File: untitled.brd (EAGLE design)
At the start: 54 x 54 mm, 22 parts, among them IC1 SN65220DBV, J3 CORTEX_DEBUG_PTH, J6 USB-MICROB, U1 ATSAMD21G-M, U2 MIC5501-3.0YM5-TR

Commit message: added vias below bus connectors
added vias below bus connectors to improve mechanical stability. Added ground symbol on bus connection net.
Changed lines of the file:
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@@
 <wire x1="41.1" y1="10" x2="41.07" y2="9.97" width="0.254" layer="16"/>
+</signal>
+<signal name="N$2">
+<via x="51.45" y="39.2" extent="1-16" drill="0.35"/>
+</signal>
+<signal name="N$3">
+<via x="52.5" y="39.2" extent="1-16" drill="0.35"/>
+</signal>
+<signal name="N$5">
+<via x="51.45" y="44.8" extent="1-16" drill="0.35"/>
+</signal>
+<signal name="N$6">
+<via x="52.5" y="44.8" extent="1-16" drill="0.35"/>
+</signal>
+<signal name="N$7">
+<via x="1.5" y="44.8" extent="1-16" drill="0.35"/>
+</signal>
+<signal name="N$8">
+<via x="2.55" y="44.8" extent="1-16" drill="0.35"/>
+</signal>
+<signal name="N$9">
+<via x="1.5" y="39.2" extent="1-16" drill="0.35"/>
+</signal>
+<signal name="N$11">
+<via x="2.55" y="39.2" extent="1-16" drill="0.35"/>
 </signal>
 </signals>

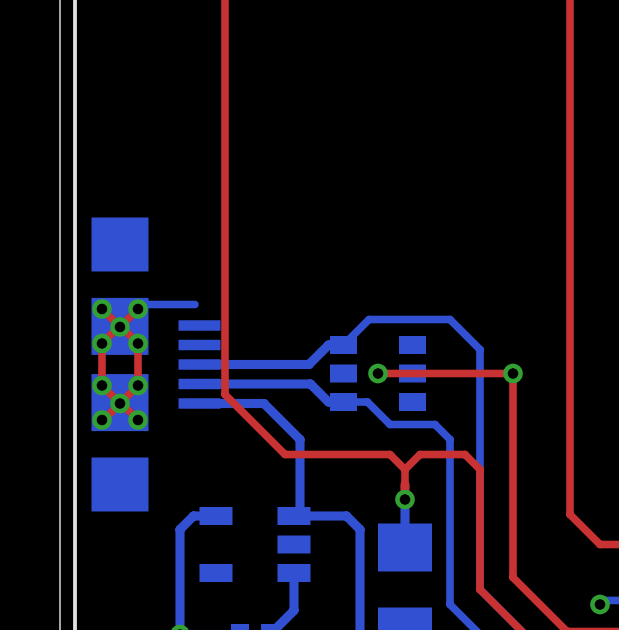
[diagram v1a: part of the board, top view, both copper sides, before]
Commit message: fixed wire stub drc error
removed wire stub on the USB connection vias.
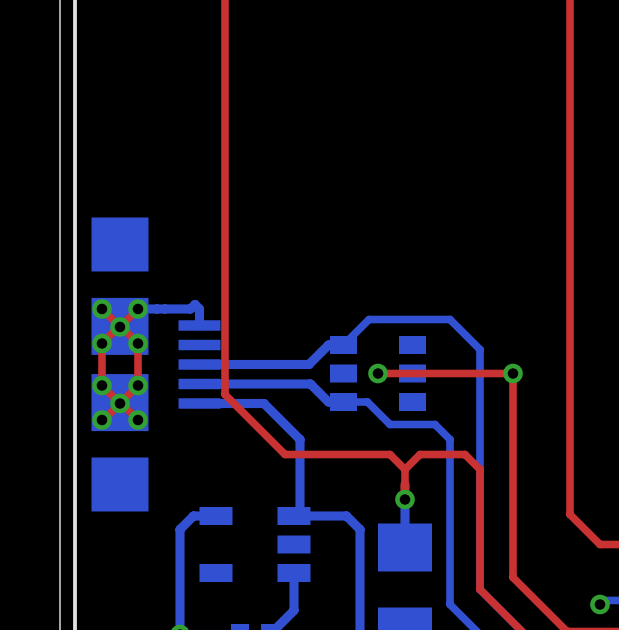
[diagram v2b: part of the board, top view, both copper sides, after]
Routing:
- net GND: track 40.6 -> 41.4 mm
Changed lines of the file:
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@@
 <wire x1="1.45" y1="17.65" x2="1.4" y2="17.65" width="0.254" layer="1"/>
 <wire x1="2" y1="18.2" x2="1.4" y2="18.8" width="0.254" layer="1"/>
-<wire x1="2.6" y1="21.35" x2="2.75" y2="21.5" width="0.254" layer="16"/>
-<wire x1="2.75" y1="21.5" x2="4.5" y2="21.5" width="0.254" layer="16"/>
+<wire x1="4.65" y1="20.8" x2="4.65" y2="21.35" width="0.3048" layer="16"/>
+<wire x1="4.65" y1="21.35" x2="4.5" y2="21.5" width="0.3048" layer="16"/>
+<wire x1="4.5" y1="21.5" x2="4.35" y2="21.35" width="0.3048" layer="16"/>
+<wire x1="4.35" y1="21.35" x2="3.5" y2="21.35" width="0.3048" layer="16"/>
+<wire x1="3.5" y1="21.35" x2="3.2294" y2="21.35" width="0.3048" layer="16"/>
+<wire x1="2.6" y1="21.35" x2="3.2294" y2="21.35" width="0.3048" layer="16"/>
 </signal>
 <signal name="1W">

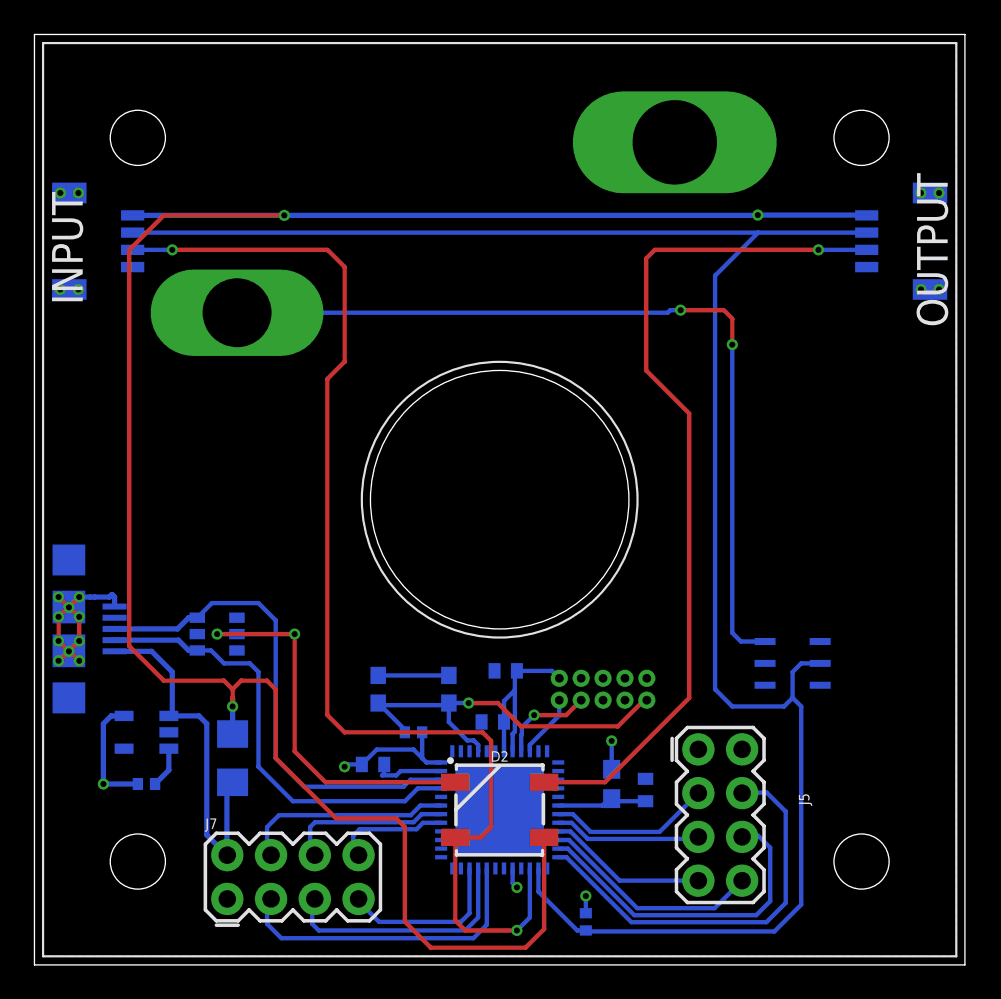
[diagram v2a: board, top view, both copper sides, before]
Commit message: changed button from 3v to 5v
moved button from 3v to 5v as the ds2413 is 5v tolerant and 5v is passed via the bus connector while 3v is not. Also negates the need for a vreg on each board.
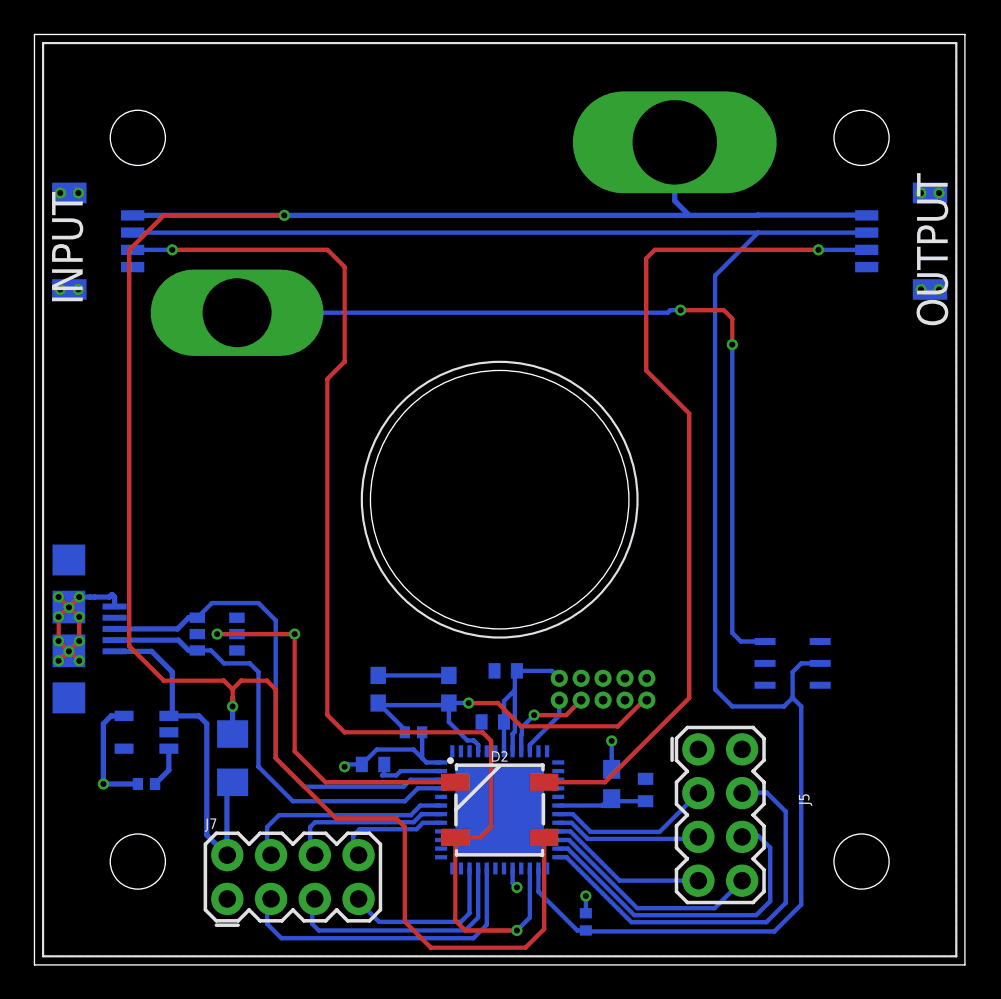
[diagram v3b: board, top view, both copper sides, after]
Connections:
- net 5V: now also U$1.P$3
- net VCC: no longer U$1.P$3
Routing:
- net 5V: track 121.6 -> 125.7 mm, vias 3 -> 2
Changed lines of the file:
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@@
 <contactref element="U1" pad="36"/>
 <contactref element="C6" pad="1"/>
-<contactref element="U$1" pad="P$3"/>
 <wire x1="23.6" y1="11.75" x2="22.75" y2="11.75" width="0.254" layer="16"/>
 <wire x1="22.75" y1="11.75" x2="22.5" y2="12" width="0.254" layer="16"/>
@@
 <contactref element="J2" pad="1"/>
 <contactref element="D2" pad="1"/>
-<via x="41.981125" y="43.518875" extent="1-16" drill="0.35"/>
 <wire x1="48.3" y1="43.518875" x2="41.981125" y2="43.518875" width="0.3048" layer="16"/>
 <contactref element="J1" pad="4"/>
 <wire x1="14.5" y1="43.5" x2="5.7" y2="43.5" width="0.3048" layer="16"/>
-<wire x1="14.5" y1="43.5" x2="41.96225" y2="43.5" width="0.3048" layer="16"/>
-<wire x1="41.96225" y1="43.5" x2="41.981125" y2="43.518875" width="0.254" layer="16"/>
+<wire x1="14.5" y1="43.5" x2="38" y2="43.5" width="0.3048" layer="16"/>
+<wire x1="38" y1="43.5" x2="41.96225" y2="43.5" width="0.3048" layer="16"/>
 <wire x1="48.3" y1="43.5" x2="48.3" y2="43.518875" width="0.3048" layer="16"/>
 <via x="14.5" y="43.5" extent="1-16" drill="0.35"/>
@@
 <wire x1="23" y1="1" x2="21.5" y2="2.5" width="0.254" layer="1"/>
 <wire x1="21" y1="8.5" x2="17.5" y2="8.5" width="0.254" layer="1"/>
-<wire x1="11.5" y1="15" x2="11.5" y2="15.5" width="0.254" layer="1"/>
 <wire x1="11.5" y1="16" x2="11" y2="16.5" width="0.254" layer="1"/>
 <wire x1="11" y1="16.5" x2="7.5" y2="16.5" width="0.254" layer="1"/>
@@
 <wire x1="7.5" y1="16.5" x2="5.5" y2="18.5" width="0.254" layer="1"/>
 <wire x1="5.5" y1="18.5" x2="5.5" y2="41.5" width="0.254" layer="1"/>
+<contactref element="U$1" pad="P$3"/>
+<wire x1="38" y1="43.5" x2="37.16" y2="44.34" width="0.3048" layer="16"/>
+<wire x1="37.16" y1="44.34" x2="37.16" y2="47.74" width="0.3048" layer="16"/>
+<wire x1="41.981125" y1="43.518875" x2="41.96225" y2="43.5" width="0.3048" layer="16"/>
 </signal>
 <signal name="N$1">

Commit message: Rev 1 error fixes
Updated ldo pull up resistor to Vin. Moved part values to layer that will show up in silkscreen. Updated capacitor footprint to match proper 0402 sizing. Replaced usb tvs/res IC. increased pullback.
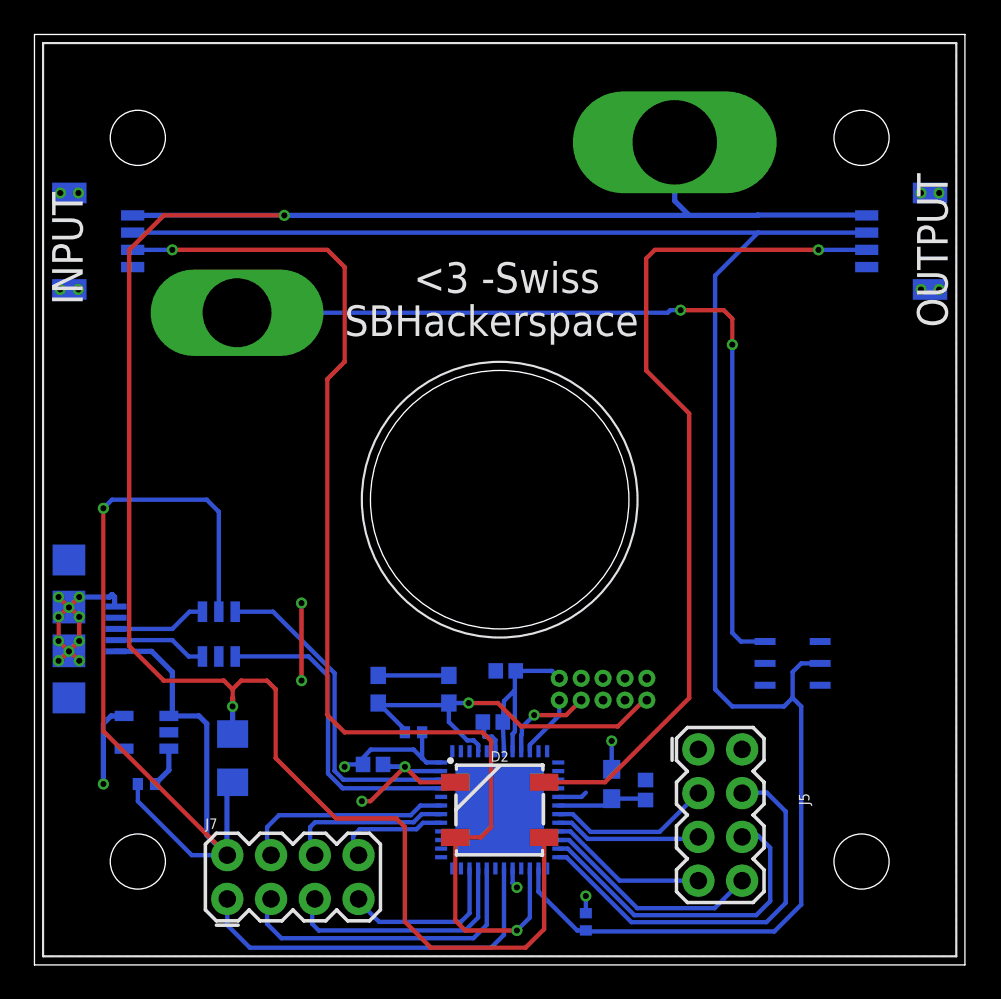
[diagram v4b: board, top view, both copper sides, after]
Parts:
- removed IC1: SN65220DBV, sn65220_40:SOT23-6
- added U3: TPD2S017, SparkFun-IC-Conversion:SOT23-6
- C1, C2, C6: value .1f -> 0.1uF; device resistor:C0402 -> SparkFun-Capacitors:0402
- C3: value .1f -> .1uF; device resistor:C0402 -> SparkFun-Capacitors:0402
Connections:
- removed net D+: IC1.6, J6.D+, U1.34
- removed net D-: IC1.4, J6.D-, U1.33
- new net DI+: J6.D+, U3.4
- new net DI-: J6.D-, U3.3
- new net DO+: U1.34, U3.6
- new net DO-: U1.33, U3.1
- net GND: now also U3.2; no longer IC1.2, IC1.5
- net VBUS: now also R3.2, U3.5
- net VCC: no longer R3.2
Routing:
- net VBUS: track 21.4 -> 64.9 mm, vias 0 -> 1
- net D+: track 28.8 -> 0.00 mm
- net D-: track 26.4 -> 0.00 mm
- net DO+: track 0.00 -> 19.3 mm
- net DO-: track 0.00 -> 18.4 mm
- net GND: track 41.4 -> 58.5 mm, vias 12 -> 14
- net DI+: track 0.00 -> 5.51 mm
- net DI-: track 0.00 -> 5.49 mm
- net VCC: track 29.8 -> 28.2 mm
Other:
- board text added: "<3 -Swiss"
- board text added: "SBHackerspace"
